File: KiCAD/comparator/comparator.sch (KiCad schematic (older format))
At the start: 12 parts, among them J1 Output, J2 Input, U1 TLC3704, U2 TLC3704

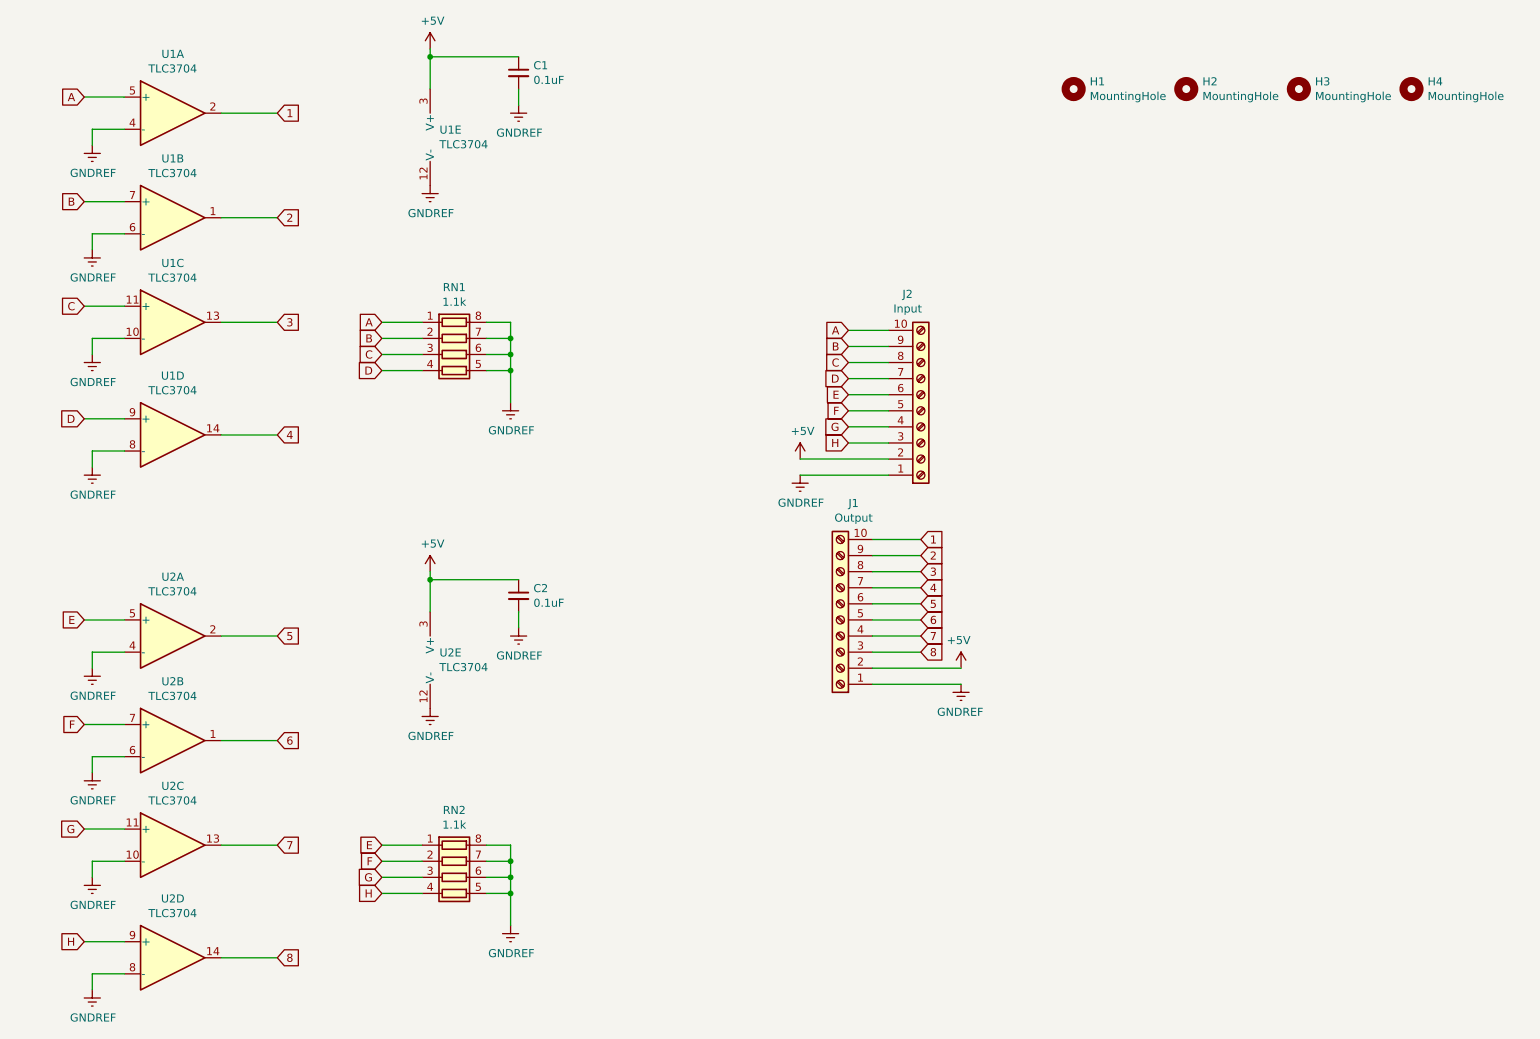
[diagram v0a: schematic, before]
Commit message: Added a tweaker pot for sensitivity testing
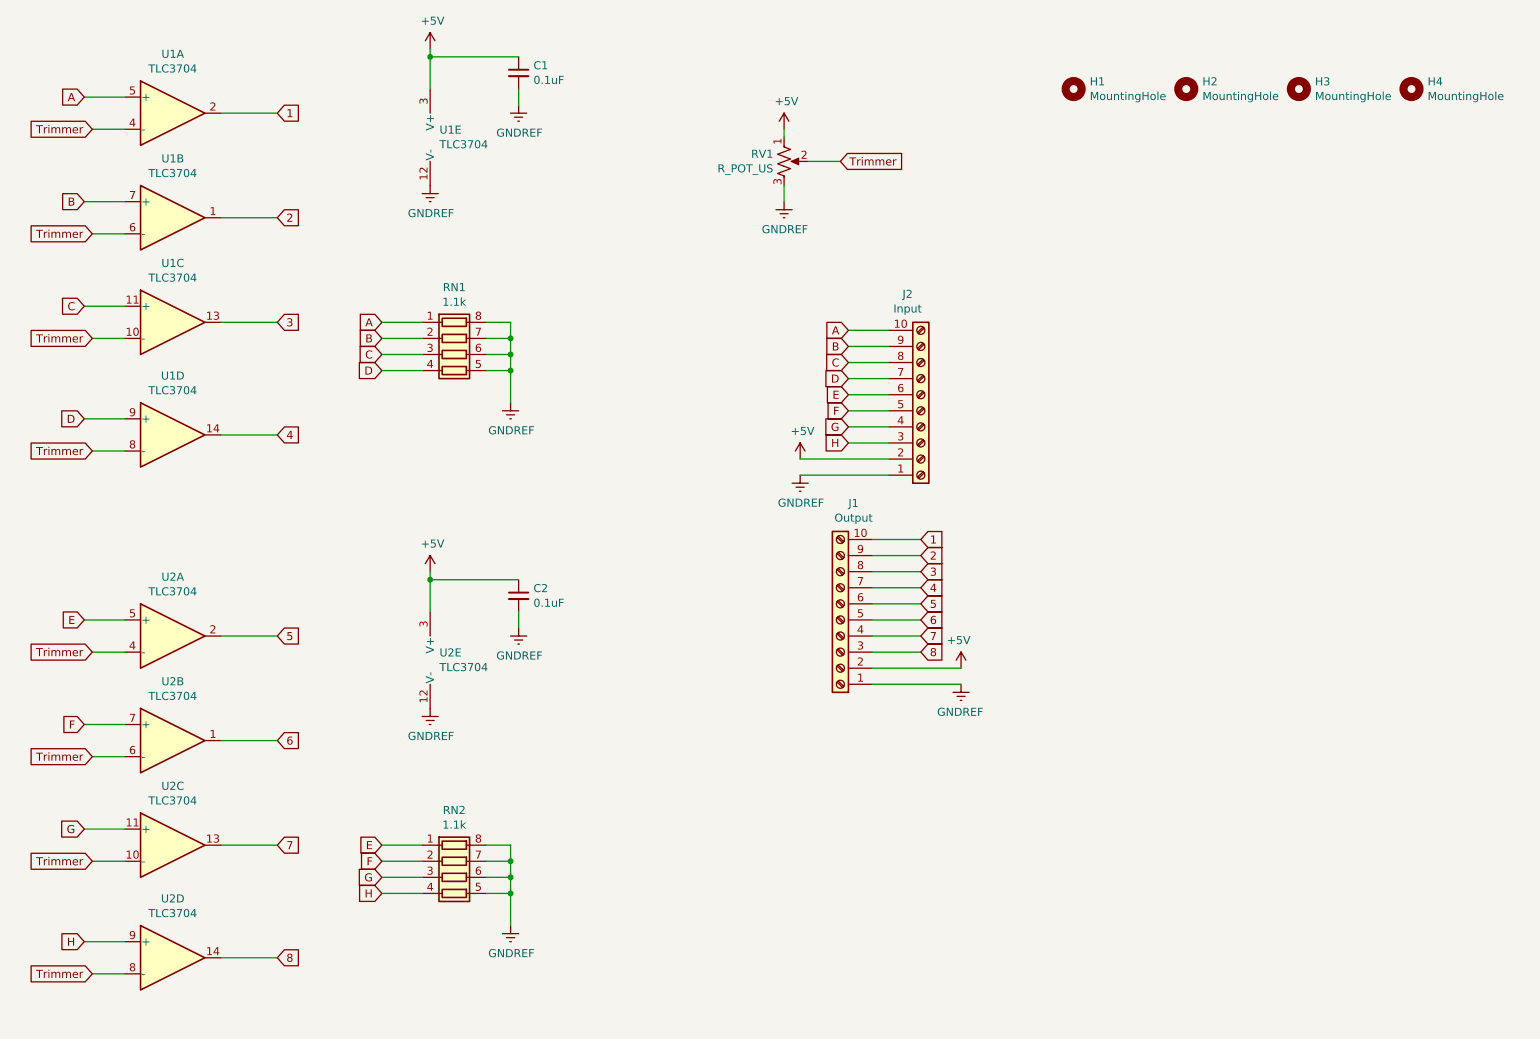
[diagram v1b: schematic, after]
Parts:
- added RV1: R_POT_US, pot_TT:P120PK-Y25BR10K, symbol Device:R_POT_US
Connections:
- net +5V: now also RV1.1
- net GNDREF: now also RV1.3; no longer U1.10 (-), U1.4 (-), U1.6 (-), U1.8 (-), U2.10 (-), U2.4 (-), U2.6 (-), U2.8 (-)
- new net Trimmer: RV1.2, U1.10 (-), U1.4 (-), U1.6 (-), U1.8 (-), U2.10 (-), U2.4 (-), U2.6 (-), U2.8 (-)
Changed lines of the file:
@@
 Wire Wire Line
 	1150 3100 1400 3100
-$Comp
-L power:GNDREF #PWR01
-U 1 1 5F20588F
-P 1200 1400
-F 0 "#PWR01" H 1200 1150 50  0001 C CNN
-F 1 "GNDREF" H 1205 1227 50  0000 C CNN
-F 2 "" H 1200 1400 50  0001 C CNN
-F 3 "" H 1200 1400 50  0001 C CNN
-	1    1200 1400
-	1    0    0    -1
-$EndComp
-Wire Wire Line
-	1200 1300 1200 1400
 Wire Wire Line
 	1200 1300 1400 1300
-$Comp
-L power:GNDREF #PWR02
-U 1 1 5F206AE1
-P 1200 2050
-F 0 "#PWR02" H 1200 1800 50  0001 C CNN
-F 1 "GNDREF" H 1205 1877 50  0000 C CNN
-F 2 "" H 1200 2050 50  0001 C CNN
-F 3 "" H 1200 2050 50  0001 C CNN
-	1    1200 2050
-	1    0    0    -1
-$EndComp
-Wire Wire Line
-	1200 1950 1200 2050
-Wire Wire Line
-	1200 1950 1400 1950
-$Comp
-L power:GNDREF #PWR03
-U 1 1 5F207444
-P 1200 2700
-F 0 "#PWR03" H 1200 2450 50  0001 C CNN
-F 1 "GNDREF" H 1205 2527 50  0000 C CNN
-F 2 "" H 1200 2700 50  0001 C CNN
-F 3 "" H 1200 2700 50  0001 C CNN
-	1    1200 2700
-	1    0    0    -1
-$EndComp
-Wire Wire Line
-	1200 2600 1200 2700
-Wire Wire Line
-	1200 2600 1400 2600
-$Comp
-L power:GNDREF #PWR04
-U 1 1 5F207D91
-P 1200 3400
-F 0 "#PWR04" H 1200 3150 50  0001 C CNN
-F 1 "GNDREF" H 1205 3227 50  0000 C CNN
-F 2 "" H 1200 3400 50  0001 C CNN
-F 3 "" H 1200 3400 50  0001 C CNN
-	1    1200 3400
-	1    0    0    -1
-$EndComp
-Wire Wire Line
-	1200 3300 1200 3400
-Wire Wire Line
-	1200 3300 1400 3300
 Text GLabel 2350 1200 2    50   Input ~ 0
 1
@@
 Wire Wire Line
 	1150 6350 1400 6350
-$Comp
-L power:GNDREF #PWR05
-U 1 1 5F21807D
-P 1200 4650
-F 0 "#PWR05" H 1200 4400 50  0001 C CNN
-F 1 "GNDREF" H 1205 4477 50  0000 C CNN
-F 2 "" H 1200 4650 50  0001 C CNN
-F 3 "" H 1200 4650 50  0001 C CNN
-	1    1200 4650
-	1    0    0    -1
-$EndComp
-Wire Wire Line
-	1200 4550 1200 4650
-Wire Wire Line
-	1200 4550 1400 4550
-$Comp
-L power:GNDREF #PWR06
-U 1 1 5F218085
-P 1200 5300
-F 0 "#PWR06" H 1200 5050 50  0001 C CNN
-F 1 "GNDREF" H 1205 5127 50  0000 C CNN
-F 2 "" H 1200 5300 50  0001 C CNN
-F 3 "" H 1200 5300 50  0001 C CNN
-	1    1200 5300
-	1    0    0    -1
-$EndComp
-Wire Wire Line
-	1200 5200 1200 5300
-Wire Wire Line
-	1200 5200 1400 5200
-$Comp
-L power:GNDREF #PWR07
-U 1 1 5F21808D
-P 1200 5950
-F 0 "#PWR07" H 1200 5700 50  0001 C CNN
-F 1 "GNDREF" H 1205 5777 50  0000 C CNN
-F 2 "" H 1200 5950 50  0001 C CNN
-F 3 "" H 1200 5950 50  0001 C CNN
-	1    1200 5950
-	1    0    0    -1
-$EndComp
-Wire Wire Line
-	1200 5850 1200 5950
-Wire Wire Line
-	1200 5850 1400 5850
-$Comp
-L power:GNDREF #PWR08
-U 1 1 5F218095
-P 1200 6650
-F 0 "#PWR08" H 1200 6400 50  0001 C CNN
-F 1 "GNDREF" H 1205 6477 50  0000 C CNN
-F 2 "" H 1200 6650 50  0001 C CNN
-F 3 "" H 1200 6650 50  0001 C CNN
-	1    1200 6650
-	1    0    0    -1
-$EndComp
-Wire Wire Line
-	1200 6550 1200 6650
-Wire Wire Line
-	1200 6550 1400 6550
 Text GLabel 2350 4450 2    50   Input ~ 0
 5
@@
 	1    0    0    -1
 $EndComp
+$Comp
+L Device:R_POT_US RV1
+U 1 1 60238D69
+P 5500 1500
+F 0 "RV1" H 5433 1546 50  0000 R CNN
+F 1 "R_POT_US" H 5433 1455 50  0000 R CNN
+F 2 "pot_TT:P120PK-Y25BR10K" H 5500 1500 50  0001 C CNN
+F 3 "~" H 5500 1500 50  0001 C CNN
+	1    5500 1500
+	1    0    0    -1
+$EndComp
+$Comp
+L power:+5V #PWR01
+U 1 1 6023B582
+P 5500 1300
+F 0 "#PWR01" H 5500 1150 50  0001 C CNN
+F 1 "+5V" H 5515 1473 50  0000 C CNN
+F 2 "" H 5500 1300 50  0001 C CNN
+F 3 "" H 5500 1300 50  0001 C CNN
+	1    5500 1300
+	1    0    0    -1
+$EndComp
+Wire Wire Line
+	5500 1300 5500 1350
+$Comp
+L power:GNDREF #PWR02
+U 1 1 6023DF3D
+P 5500 1750
+F 0 "#PWR02" H 5500 1500 50  0001 C CNN
+F 1 "GNDREF" H 5505 1577 50  0000 C CNN
+F 2 "" H 5500 1750 50  0001 C CNN
+F 3 "" H 5500 1750 50  0001 C CNN
+	1    5500 1750
+	1    0    0    -1
+$EndComp
+Wire Wire Line
+	5500 1650 5500 1750
+Text GLabel 1200 1300 0    50   Input ~ 0
+Trimmer
+Wire Wire Line
+	1200 1950 1400 1950
+Text GLabel 1200 1950 0    50   Input ~ 0
+Trimmer
+Wire Wire Line
+	1200 2600 1400 2600
+Text GLabel 1200 2600 0    50   Input ~ 0
+Trimmer
+Wire Wire Line
+	1200 3300 1400 3300
+Text GLabel 1200 3300 0    50   Input ~ 0
+Trimmer
+Wire Wire Line
+	1200 4550 1400 4550
+Text GLabel 1200 4550 0    50   Input ~ 0
+Trimmer
+Wire Wire Line
+	1200 5200 1400 5200
+Text GLabel 1200 5200 0    50   Input ~ 0
+Trimmer
+Wire Wire Line
+	1200 5850 1400 5850
+Text GLabel 1200 5850 0    50   Input ~ 0
+Trimmer
+Wire Wire Line
+	1200 6550 1400 6550
+Text GLabel 1200 6550 0    50   Input ~ 0
+Trimmer
+Wire Wire Line
+	5850 1500 5650 1500
+Text GLabel 5850 1500 2    50   Input ~ 0
+Trimmer
 $EndSCHEMATC
